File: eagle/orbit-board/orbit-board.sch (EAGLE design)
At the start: 1 part

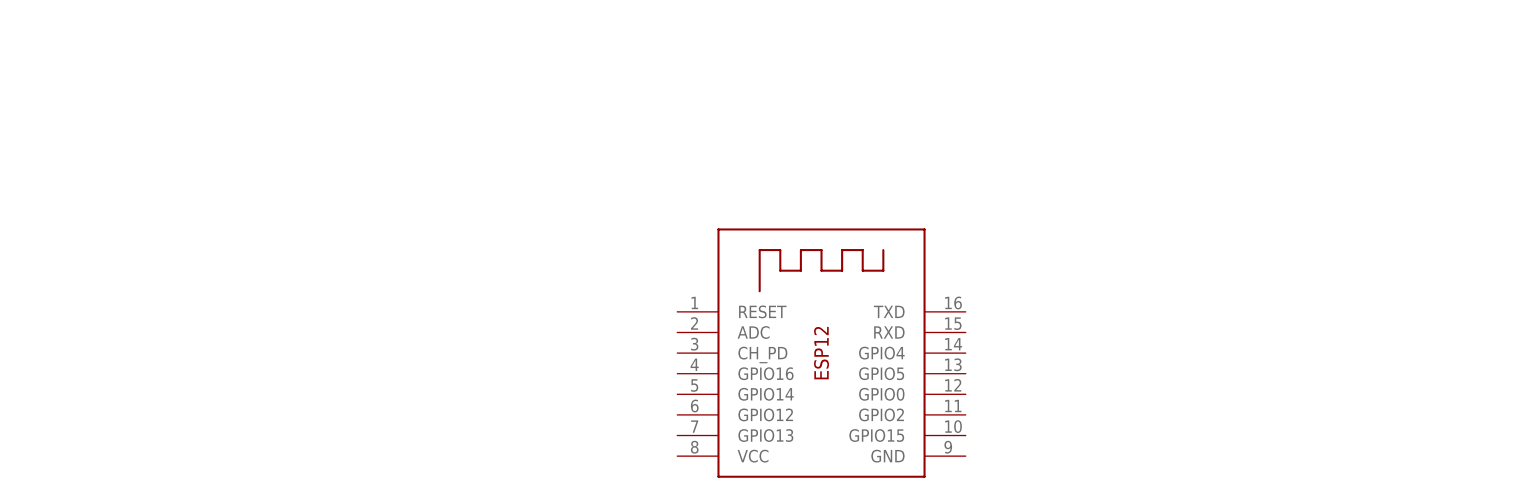
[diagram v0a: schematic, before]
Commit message: added programming header and LDO 3.3V regulator
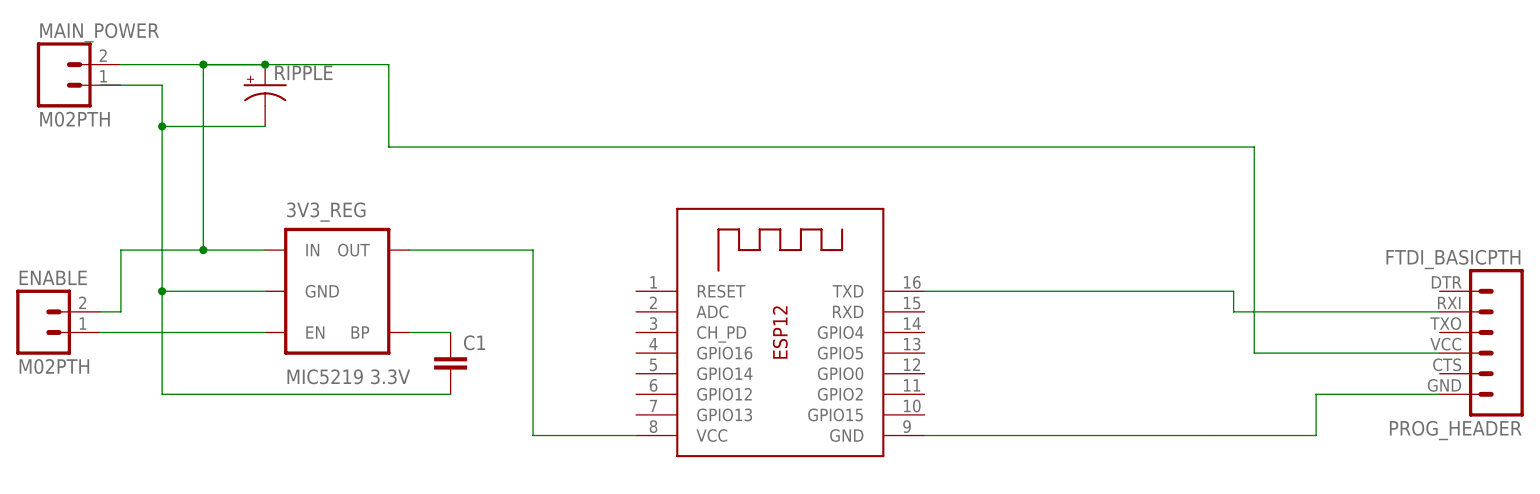
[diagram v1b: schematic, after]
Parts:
- added 3V3_REG: MIC5219 3.3V, SparkFun-PowerIC:V_REG_MIC52193.3V
- added C1: (no value), SparkFun-Capacitors:CAP1210
- added ENABLE, MAIN_POWER: M02PTH, SparkFun-Connectors:M02PTH
- added PROG_HEADER: FTDI_BASICPTH, SparkFun-Connectors:FTDI_BASICPTH
- added RIPPLE: (no value), SparkFun-Capacitors:CAP_POLPTH2
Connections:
- new net N$1: PROG_HEADER.6, X1.GND
- new net N$4: PROG_HEADER.2, X1.TXD
- new net N$5: 3V3_REG.OUT, X1.VCC
- new net N$6: 3V3_REG.IN, ENABLE.2, MAIN_POWER.2, PROG_HEADER.4, RIPPLE.+
- new net N$7: 3V3_REG.GND, C1.2, RIPPLE.-
- new net N$8: 3V3_REG.EN, ENABLE.1
- new net N$9: 3V3_REG.BP, C1.1
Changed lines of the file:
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@@
 <?xml version="1.0" encoding="utf-8"?>
 <!DOCTYPE eagle SYSTEM "eagle.dtd">
-<eagle version="7.3.0">
+<eagle version="6.3">
 <drawing>
 <settings>
@@
 <parts>
 <part name="X1" library="adafruit" deviceset="ESP-12" device=""/>
+<part name="3V3_REG" library="SparkFun-PowerIC" deviceset="V_REG_MIC5219" device="3.3V" value="MIC5219 3.3V"/>
+<part name="PROG_HEADER" library="SparkFun-Connectors" deviceset="FTDI_BASIC" device="PTH"/>
+<part name="RIPPLE" library="SparkFun-Capacitors" deviceset="CAP_POL" device="PTH2"/>
+<part name="MAIN_POWER" library="SparkFun-Connectors" deviceset="M02" device="PTH"/>
+<part name="ENABLE" library="SparkFun-Connectors" deviceset="M02" device="PTH"/>
+<part name="C1" library="SparkFun-Capacitors" deviceset="CAP" device="1210"/>
 </parts>
 <sheets>
@@
 </plain>
 <instances>
-<instance part="X1" gate="G$1" x="63.5" y="45.72"/>
+<instance part="X1" gate="G$1" x="58.42" y="48.26"/>
+<instance part="3V3_REG" gate="G$1" x="5.08" y="53.34"/>
+<instance part="PROG_HEADER" gate="G$1" x="144.78" y="48.26" rot="R180"/>
+<instance part="RIPPLE" gate="G$1" x="-5.08" y="78.74"/>
+<instance part="MAIN_POWER" gate="G$1" x="-30.48" y="78.74"/>
+<instance part="ENABLE" gate="G$1" x="-33.02" y="48.26"/>
+<instance part="C1" gate="G$1" x="17.78" y="43.18"/>
 </instances>
 <busses>
 </busses>
 <nets>
+<net name="N$1" class="0">
+<segment>
+<pinref part="PROG_HEADER" gate="G$1" pin="6"/>
+<wire x1="139.7" y1="40.64" x2="124.46" y2="40.64" width="0.1524" layer="91"/>
+<wire x1="124.46" y1="40.64" x2="124.46" y2="35.56" width="0.1524" layer="91"/>
+<wire x1="124.46" y1="35.56" x2="111.76" y2="35.56" width="0.1524" layer="91"/>
+<pinref part="X1" gate="G$1" pin="GND"/>
+<wire x1="76.2" y1="35.56" x2="111.76" y2="35.56" width="0.1524" layer="91"/>
+</segment>
+</net>
+<net name="N$4" class="0">
+<segment>
+<pinref part="PROG_HEADER" gate="G$1" pin="2"/>
+<wire x1="139.7" y1="50.8" x2="114.3" y2="50.8" width="0.1524" layer="91"/>
+<wire x1="114.3" y1="50.8" x2="114.3" y2="53.34" width="0.1524" layer="91"/>
+<pinref part="X1" gate="G$1" pin="TXD"/>
+<wire x1="114.3" y1="53.34" x2="76.2" y2="53.34" width="0.1524" layer="91"/>
+</segment>
+</net>
+<net name="N$5" class="0">
+<segment>
+<pinref part="X1" gate="G$1" pin="VCC"/>
+<wire x1="40.64" y1="35.56" x2="27.94" y2="35.56" width="0.1524" layer="91"/>
+<wire x1="27.94" y1="35.56" x2="27.94" y2="58.42" width="0.1524" layer="91"/>
+<pinref part="3V3_REG" gate="G$1" pin="OUT"/>
+<wire x1="27.94" y1="58.42" x2="12.7" y2="58.42" width="0.1524" layer="91"/>
+</segment>
+</net>
+<net name="N$6" class="0">
+<segment>
+<pinref part="MAIN_POWER" gate="G$1" pin="2"/>
+<pinref part="RIPPLE" gate="G$1" pin="+"/>
+<wire x1="-22.86" y1="81.28" x2="-12.7" y2="81.28" width="0.1524" layer="91"/>
+<wire x1="-12.7" y1="81.28" x2="-5.08" y2="81.28" width="0.1524" layer="91"/>
+<wire x1="-5.08" y1="81.28" x2="-12.7" y2="81.28" width="0.1524" layer="91"/>
+<wire x1="-12.7" y1="81.28" x2="-12.7" y2="58.42" width="0.1524" layer="91"/>
+<pinref part="3V3_REG" gate="G$1" pin="IN"/>
+<wire x1="-12.7" y1="58.42" x2="-5.08" y2="58.42" width="0.1524" layer="91"/>
+<pinref part="ENABLE" gate="G$1" pin="2"/>
+<wire x1="-25.4" y1="50.8" x2="-22.86" y2="50.8" width="0.1524" layer="91"/>
+<wire x1="-22.86" y1="50.8" x2="-22.86" y2="58.42" width="0.1524" layer="91"/>
+<wire x1="-22.86" y1="58.42" x2="-12.7" y2="58.42" width="0.1524" layer="91"/>
+<junction x="-12.7" y="58.42"/>
+<junction x="-12.7" y="81.28"/>
+<pinref part="PROG_HEADER" gate="G$1" pin="4"/>
+<wire x1="139.7" y1="45.72" x2="116.84" y2="45.72" width="0.1524" layer="91"/>
+<wire x1="116.84" y1="45.72" x2="116.84" y2="71.12" width="0.1524" layer="91"/>
+<wire x1="116.84" y1="71.12" x2="10.16" y2="71.12" width="0.1524" layer="91"/>
+<wire x1="10.16" y1="71.12" x2="10.16" y2="81.28" width="0.1524" layer="91"/>
+<wire x1="10.16" y1="81.28" x2="-5.08" y2="81.28" width="0.1524" layer="91"/>
+<junction x="-5.08" y="81.28"/>
+</segment>
+</net>
+<net name="N$7" class="0">
+<segment>
+<wire x1="-25.4" y1="78.74" x2="-17.78" y2="78.74" width="0.1524" layer="91"/>
+<wire x1="-17.78" y1="78.74" x2="-17.78" y2="73.66" width="0.1524" layer="91"/>
+<pinref part="3V3_REG" gate="G$1" pin="GND"/>
+<wire x1="-17.78" y1="73.66" x2="-17.78" y2="53.34" width="0.1524" layer="91"/>
+<wire x1="-17.78" y1="53.34" x2="-5.08" y2="53.34" width="0.1524" layer="91"/>
+<pinref part="RIPPLE" gate="G$1" pin="-"/>
+<wire x1="-5.08" y1="73.66" x2="-17.78" y2="73.66" width="0.1524" layer="91"/>
+<junction x="-17.78" y="73.66"/>
+<wire x1="-17.78" y1="53.34" x2="-17.78" y2="40.64" width="0.1524" layer="91"/>
+<pinref part="C1" gate="G$1" pin="2"/>
+<wire x1="-17.78" y1="40.64" x2="17.78" y2="40.64" width="0.1524" layer="91"/>
+<junction x="-17.78" y="53.34"/>
+</segment>
+</net>
+<net name="N$8" class="0">
+<segment>
+<pinref part="ENABLE" gate="G$1" pin="1"/>
+<pinref part="3V3_REG" gate="G$1" pin="EN"/>
+<wire x1="-25.4" y1="48.26" x2="-5.08" y2="48.26" width="0.1524" layer="91"/>
+</segment>
+</net>
+<net name="N$9" class="0">
+<segment>
+<pinref part="C1" gate="G$1" pin="1"/>
+<pinref part="3V3_REG" gate="G$1" pin="BP"/>
+<wire x1="17.78" y1="48.26" x2="12.7" y2="48.26" width="0.1524" layer="91"/>
+</segment>
+</net>
 </nets>
 </sheet>

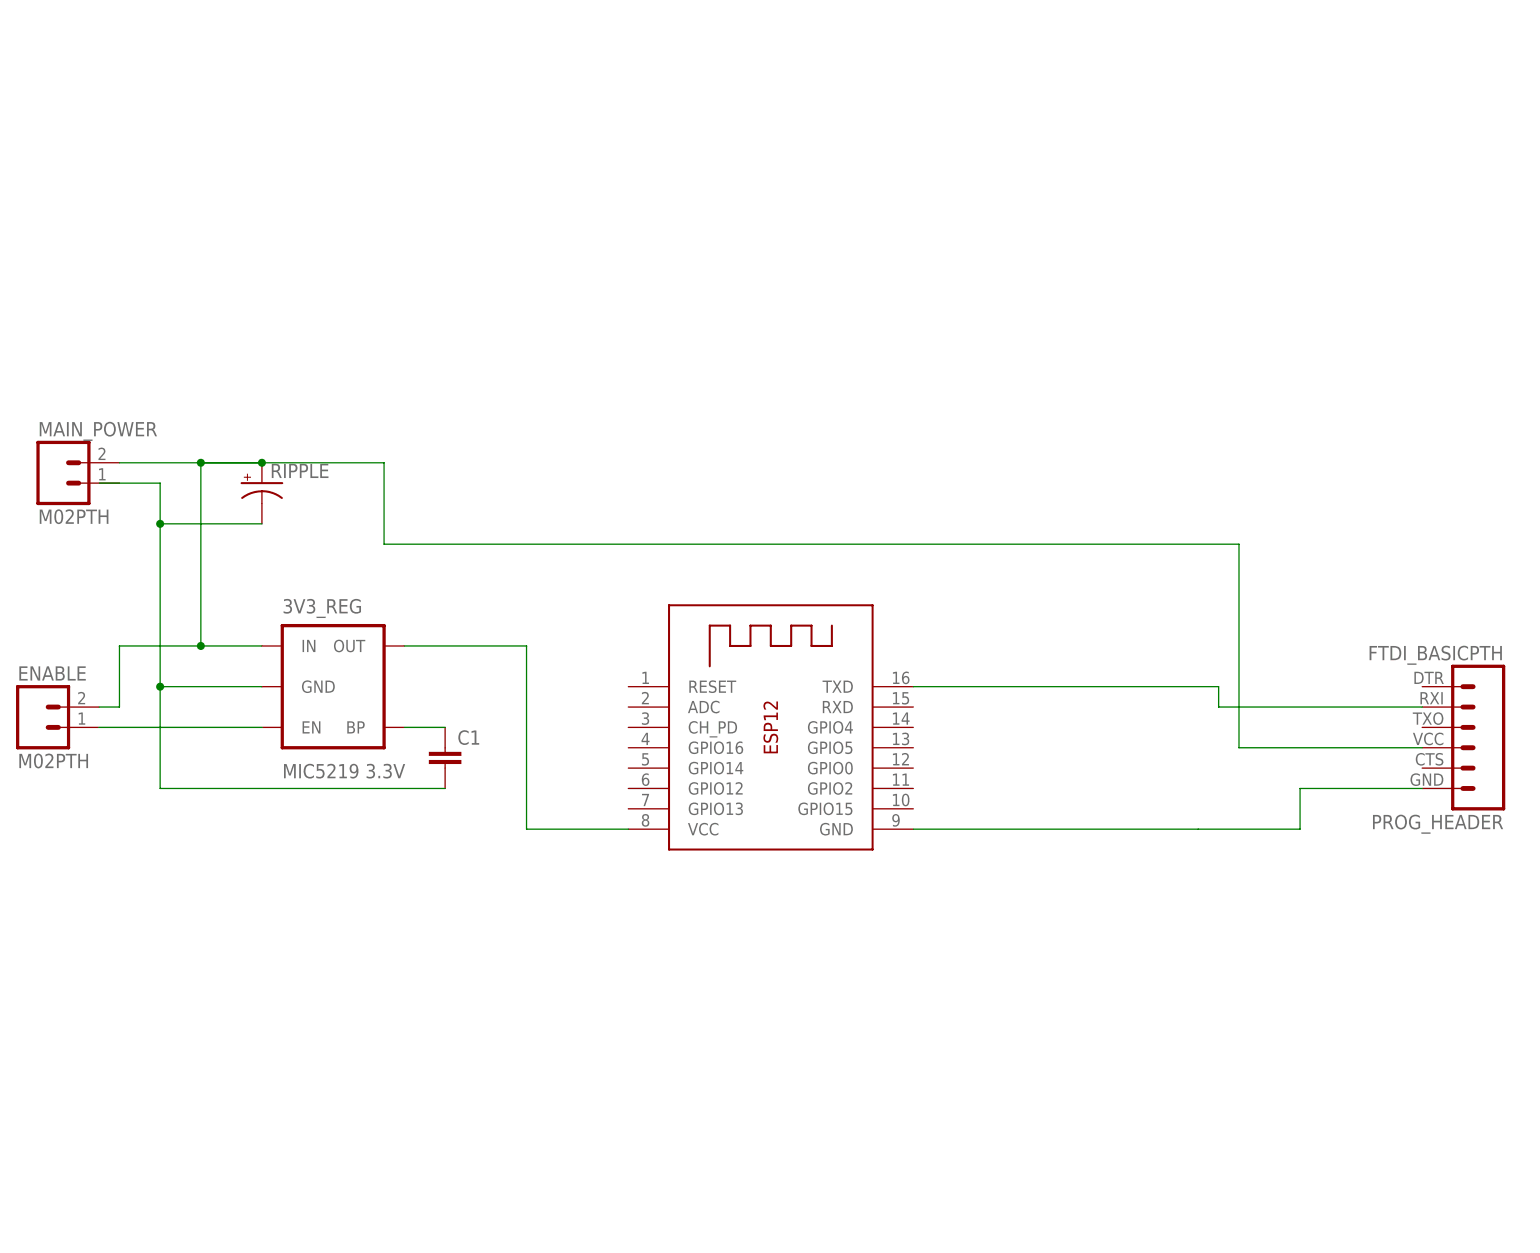
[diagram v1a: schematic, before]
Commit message: added cp2103 and mosfet for led power control
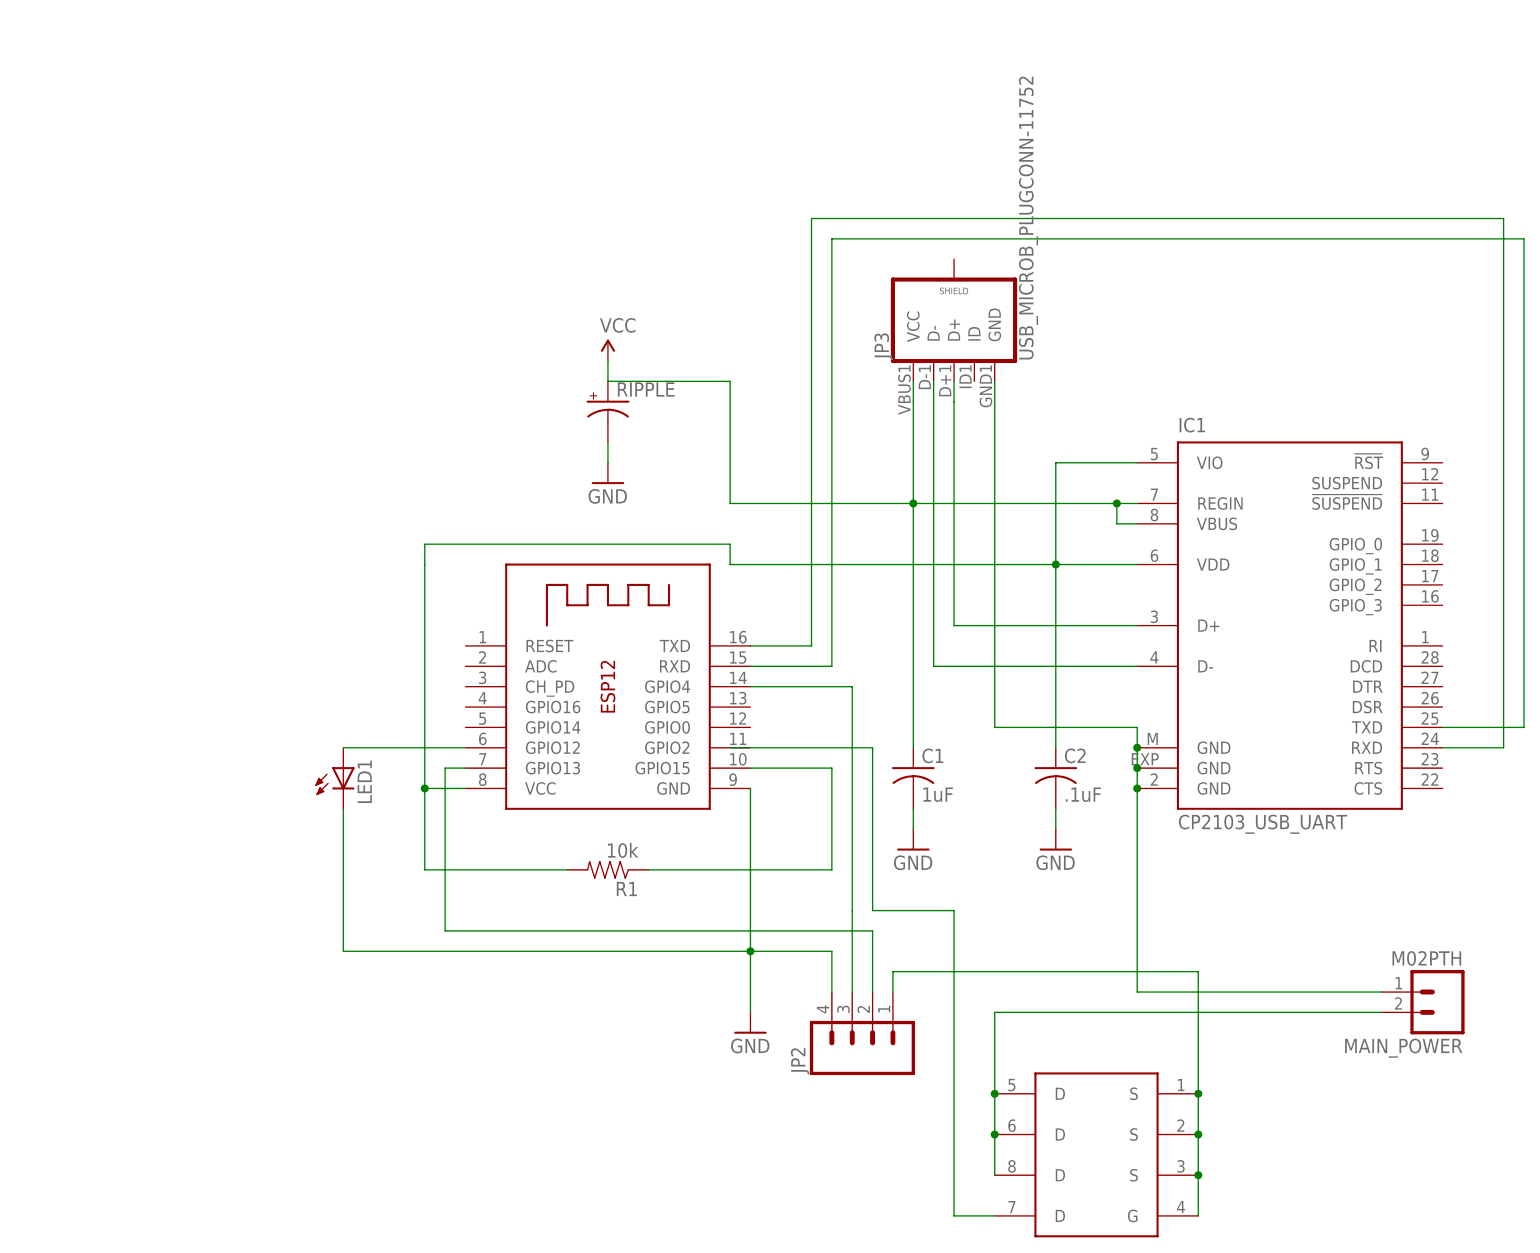
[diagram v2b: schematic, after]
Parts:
- removed 3V3_REG: MIC5219 3.3V, SparkFun-PowerIC:V_REG_MIC52193.3V
- removed ENABLE: M02PTH, SparkFun-Connectors:M02PTH
- removed PROG_HEADER: FTDI_BASICPTH, SparkFun-Connectors:FTDI_BASICPTH
- added C2: .1uF, adafruit:C-USC0603
- added IC1: CP2103_USB_UART, SparkFun-DigitalIC:CP2103_USB_UART
- added JP2: (no value), SparkFun-Connectors:M04PTH
- added JP3: USB_MICROB_PLUGCONN-11752, SparkFun-Connectors:USB_MICROB_PLUGCONN-11752
- added LED1: (no value), led:LEDSML1206
- added R1: 10k, SparkFun-Passives:RESISTOR0603-RES
- added U$1: NDS8434, SparkFun-DiscreteSemi:NDS8434
- C1: value (none) -> 1uF; device SparkFun-Capacitors:CAP1210 -> adafruit:C-USC0603
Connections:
- new net GND: C1.2, C2.2, JP2.4, LED1.C, RIPPLE.-, X1.GND
- new net N$10: R1.1, X1.GPIO15
- new net N$11: MAIN_POWER.2, U$1.D@2, U$1.D@3, U$1.D@4
- new net N$12: U$1.D@1
- new net N$14: JP2.1, U$1.G, U$1.S@1, U$1.S@2, U$1.S@3
- new net N$2: IC1.D+, JP3.D+
- new net N$3: IC1.D-, JP3.D-
- new net VCC: C1.1, IC1.REGIN, IC1.VBUS, JP3.VCC, RIPPLE.+
- net N$1: now also IC1.GND, IC1.GND@EXP, IC1.GND@M, JP3.GND, MAIN_POWER.1; no longer PROG_HEADER.6, X1.GND
- net N$4: now also C2.1, IC1.VDD, IC1.VIO, R1.2, X1.VCC; no longer PROG_HEADER.2, X1.TXD
- net N$5: now also LED1.A, X1.GPIO12; no longer 3V3_REG.OUT, X1.VCC
- net N$6: now also JP2.3, X1.GPIO4; no longer 3V3_REG.IN, ENABLE.2, MAIN_POWER.2, PROG_HEADER.4, RIPPLE.+
- net N$7: now also JP2.2, X1.GPIO13; no longer 3V3_REG.GND, C1.2, RIPPLE.-
- net N$8: now also IC1.RXD, X1.TXD; no longer 3V3_REG.EN, ENABLE.1
- net N$9: now also IC1.TXD, X1.RXD; no longer 3V3_REG.BP, C1.1
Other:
- moved on the sheet: C1, MAIN_POWER, RIPPLE

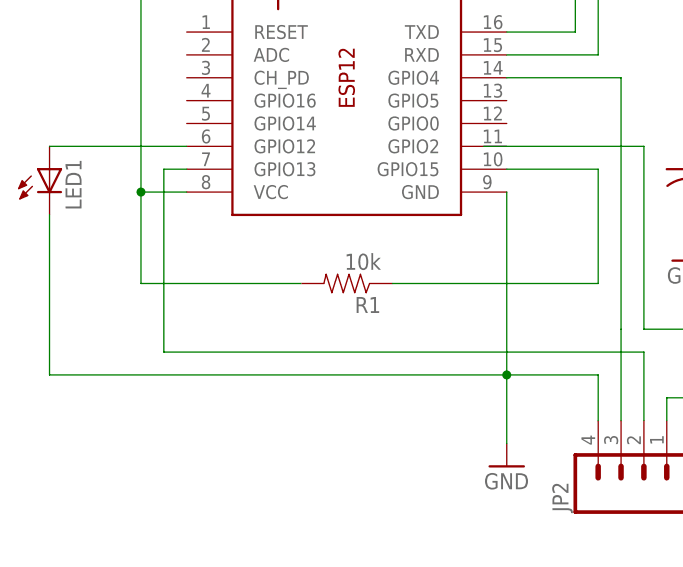
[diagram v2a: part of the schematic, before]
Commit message: fixed pulldown
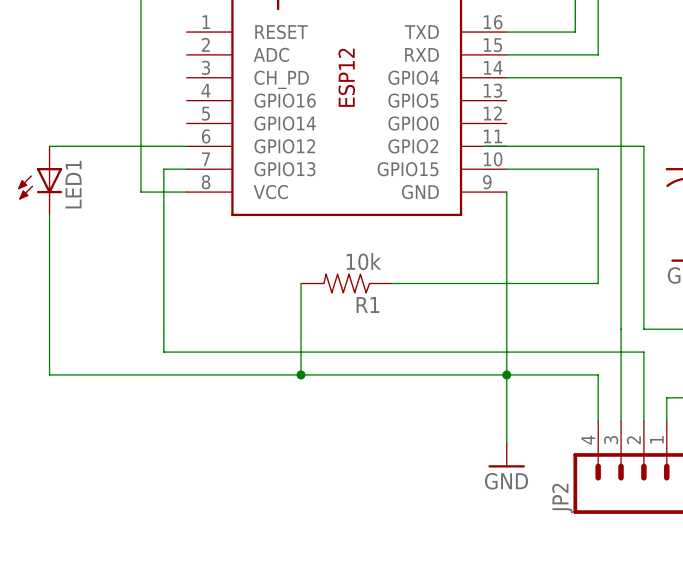
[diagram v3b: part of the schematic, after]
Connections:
- net GND: now also R1.2
- net N$4: no longer R1.2
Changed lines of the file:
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@@
 <pinref part="LED1" gate="G$1" pin="C"/>
 <wire x1="5.08" y1="38.1" x2="5.08" y2="20.32" width="0.1524" layer="91"/>
-<wire x1="5.08" y1="20.32" x2="55.88" y2="20.32" width="0.1524" layer="91"/>
+<wire x1="5.08" y1="20.32" x2="33.02" y2="20.32" width="0.1524" layer="91"/>
+<pinref part="R1" gate="G$1" pin="2"/>
+<wire x1="33.02" y1="20.32" x2="55.88" y2="20.32" width="0.1524" layer="91"/>
+<wire x1="33.02" y1="30.48" x2="33.02" y2="20.32" width="0.1524" layer="91"/>
+<junction x="33.02" y="20.32"/>
 </segment>
 <segment>
@@
 <pinref part="X1" gate="G$1" pin="VCC"/>
 <wire x1="15.24" y1="40.64" x2="20.32" y2="40.64" width="0.1524" layer="91"/>
-<pinref part="R1" gate="G$1" pin="2"/>
-<wire x1="33.02" y1="30.48" x2="15.24" y2="30.48" width="0.1524" layer="91"/>
-<wire x1="15.24" y1="30.48" x2="15.24" y2="40.64" width="0.1524" layer="91"/>
-<junction x="15.24" y="40.64"/>
 </segment>
 </net>
